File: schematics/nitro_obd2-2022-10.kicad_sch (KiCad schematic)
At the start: 16 parts

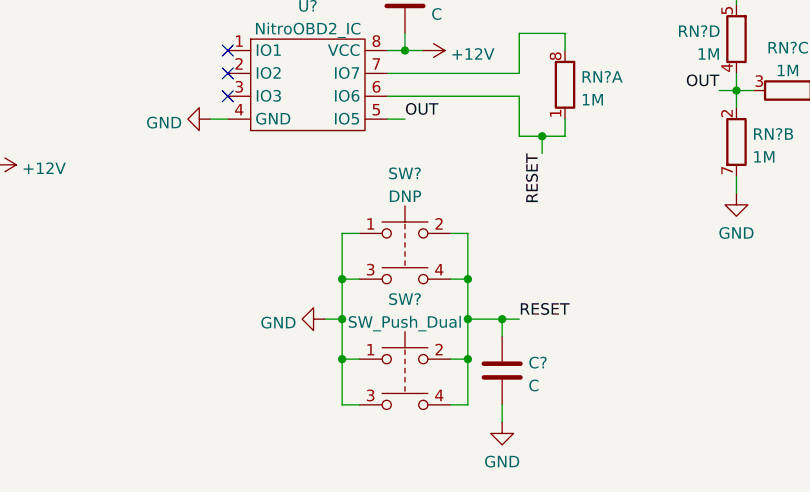
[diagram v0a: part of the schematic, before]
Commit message: Change switch for nitroOBD2 2022-09
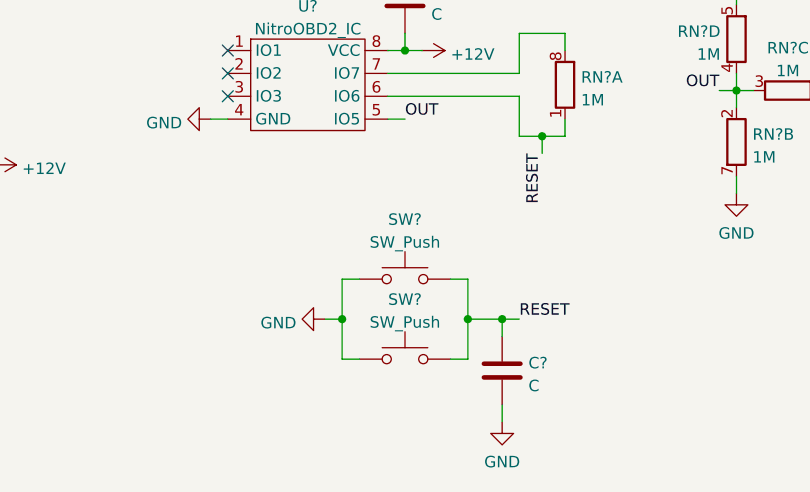
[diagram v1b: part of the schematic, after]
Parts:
- removed SW?: SW_Push_Dual, symbol Switch:SW_Push_Dual
- removed SW?: DNP, symbol Switch:SW_Push_Dual
- added SW? (x2): SW_Push, symbol Switch:SW_Push
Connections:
- net GND: now also SW?.1, SW?.1
- net RESET: now also SW?.2, SW?.2
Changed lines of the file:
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@@
   (junction (at 161.29 123.825) (diameter 0) (color 0 0 0 0)
   )
-  (junction (at 147.32 128.27) (diameter 0) (color 0 0 0 0)
-  )
-  (junction (at 147.32 119.38) (diameter 0) (color 0 0 0 0)
-  )
   (junction (at 191.135 98.425) (diameter 0) (color 0 0 0 0)
   )
@@
   )
   (junction (at 154.305 93.98) (diameter 0) (color 0 0 0 0)
-  )
-  (junction (at 161.29 128.27) (diameter 0) (color 0 0 0 0)
-  )
-  (junction (at 161.29 119.38) (diameter 0) (color 0 0 0 0)
   )
   (junction (at 169.545 103.505) (diameter 0) (color 0 0 0 0)
@@
     (stroke (width 0) (type default) (color 0 0 0 0))
   )
-  (wire (pts (xy 161.29 133.35) (xy 159.385 133.35))
-    (stroke (width 0) (type default) (color 0 0 0 0))
-  )
   (wire (pts (xy 169.545 103.505) (xy 172.085 103.505))
     (stroke (width 0) (type default) (color 0 0 0 0))
@@
     (stroke (width 0) (type default) (color 0 0 0 0))
   )
-  (wire (pts (xy 149.225 114.3) (xy 147.32 114.3))
-    (stroke (width 0) (type default) (color 0 0 0 0))
-  )
-  (wire (pts (xy 161.29 128.27) (xy 161.29 133.35))
-    (stroke (width 0) (type default) (color 0 0 0 0))
-  )
   (wire (pts (xy 154.305 93.98) (xy 156.21 93.98))
     (stroke (width 0) (type default) (color 0 0 0 0))
@@
     (stroke (width 0) (type default) (color 0 0 0 0))
   )
-  (wire (pts (xy 159.385 114.3) (xy 161.29 114.3))
-    (stroke (width 0) (type default) (color 0 0 0 0))
-  )
   (wire (pts (xy 191.135 86.995) (xy 191.135 88.9))
     (stroke (width 0) (type default) (color 0 0 0 0))
@@
     (stroke (width 0) (type default) (color 0 0 0 0))
   )
-  (wire (pts (xy 147.32 133.35) (xy 149.225 133.35))
-    (stroke (width 0) (type default) (color 0 0 0 0))
-  )
   (wire (pts (xy 161.29 119.38) (xy 161.29 123.825))
     (stroke (width 0) (type default) (color 0 0 0 0))
@@
     (stroke (width 0) (type default) (color 0 0 0 0))
   )
-  (wire (pts (xy 147.32 128.27) (xy 147.32 133.35))
-    (stroke (width 0) (type default) (color 0 0 0 0))
-  )
   (wire (pts (xy 204.47 97.79) (xy 204.47 98.425))
     (stroke (width 0) (type default) (color 0 0 0 0))
@@
     (stroke (width 0) (type default) (color 0 0 0 0))
   )
-  (wire (pts (xy 161.29 114.3) (xy 161.29 119.38))
-    (stroke (width 0) (type default) (color 0 0 0 0))
-  )
   (wire (pts (xy 204.47 109.22) (xy 204.47 111.125))
-    (stroke (width 0) (type default) (color 0 0 0 0))
-  )
-  (wire (pts (xy 147.32 114.3) (xy 147.32 119.38))
     (stroke (width 0) (type default) (color 0 0 0 0))
   )
@@
     )
     (pin "1")
-  )
-  (symbol (lib_id "Switch:SW_Push_Dual") (at 154.305 128.27 0) (unit 1)
-    (in_bom yes) (on_board yes) (fields_autoplaced)
-    (property "Reference" "SW?" (id 0) (at 154.305 121.6492 0))
-    (property "Value" "SW_Push_Dual" (id 1) (at 154.305 124.1861 0))
-    (property "Footprint" "" (id 2) (at 154.305 123.19 0)
-      (effects (font (size 1.27 1.27)) hide)
-    )
-    (property "Datasheet" "~" (id 3) (at 154.305 123.19 0)
-      (effects (font (size 1.27 1.27)) hide)
-    )
-    (pin "1")
-    (pin "2")
-    (pin "3")
-    (pin "4")
   )
   (symbol (lib_id "misc_ics:NitroOBD2_IC") (at 143.51 97.79 0) (unit 1)
@@
     (pin "1")
   )
-  (symbol (lib_id "Switch:SW_Push_Dual") (at 154.305 114.3 0) (unit 1)
-    (in_bom yes) (on_board yes) (fields_autoplaced)
-    (property "Reference" "SW?" (id 0) (at 154.305 107.6792 0))
-    (property "Value" "DNP" (id 1) (at 154.305 110.2161 0))
-    (property "Footprint" "" (id 2) (at 154.305 109.22 0)
-      (effects (font (size 1.27 1.27)) hide)
-    )
-    (property "Datasheet" "~" (id 3) (at 154.305 109.22 0)
-      (effects (font (size 1.27 1.27)) hide)
-    )
-    (pin "1")
-    (pin "2")
-    (pin "3")
-    (pin "4")
-  )
   (symbol (lib_id "power:+12V") (at 191.135 86.995 0) (unit 1)
     (in_bom yes) (on_board yes) (fields_autoplaced)
@@
     )
     (pin "1")
+  )
+  (symbol (lib_id "Switch:SW_Push") (at 154.305 119.38 0) (unit 1)
+    (in_bom yes) (on_board yes) (fields_autoplaced)
+    (property "Reference" "SW?" (id 0) (at 154.305 112.7592 0))
+    (property "Value" "SW_Push" (id 1) (at 154.305 115.2961 0))
+    (property "Footprint" "" (id 2) (at 154.305 114.3 0)
+      (effects (font (size 1.27 1.27)) hide)
+    )
+    (property "Datasheet" "~" (id 3) (at 154.305 114.3 0)
+      (effects (font (size 1.27 1.27)) hide)
+    )
+    (pin "1")
+    (pin "2")
+  )
+  (symbol (lib_id "Switch:SW_Push") (at 154.305 128.27 0) (unit 1)
+    (in_bom yes) (on_board yes) (fields_autoplaced)
+    (property "Reference" "SW?" (id 0) (at 154.305 121.6492 0))
+    (property "Value" "SW_Push" (id 1) (at 154.305 124.1861 0))
+    (property "Footprint" "" (id 2) (at 154.305 123.19 0)
+      (effects (font (size 1.27 1.27)) hide)
+    )
+    (property "Datasheet" "~" (id 3) (at 154.305 123.19 0)
+      (effects (font (size 1.27 1.27)) hide)
+    )
+    (pin "1")
+    (pin "2")
   )
   (symbol (lib_id "Device:LED") (at 204.47 105.41 90) (mirror x) (unit 1)
@@
       (reference "RN?") (unit 4) (value "1M") (footprint "")
     )
-    (path "/4a957199-98ca-4d7c-847f-f79ccd0d485c"
-      (reference "SW?") (unit 1) (value "SW_Push_Dual") (footprint "")
-    )
-    (path "/da89d813-e669-4b77-9a4b-1d281c279ba8"
-      (reference "SW?") (unit 1) (value "DNP") (footprint "")
+    (path "/df0c7818-7f02-4c3d-9906-b3ee4d910b10"
+      (reference "SW?") (unit 1) (value "SW_Push") (footprint "")
+    )
+    (path "/e3f5d89d-015c-4144-b939-911526431744"
+      (reference "SW?") (unit 1) (value "SW_Push") (footprint "")
     )
     (path "/51947fb1-f892-4830-93a8-2e54da9ee49f"

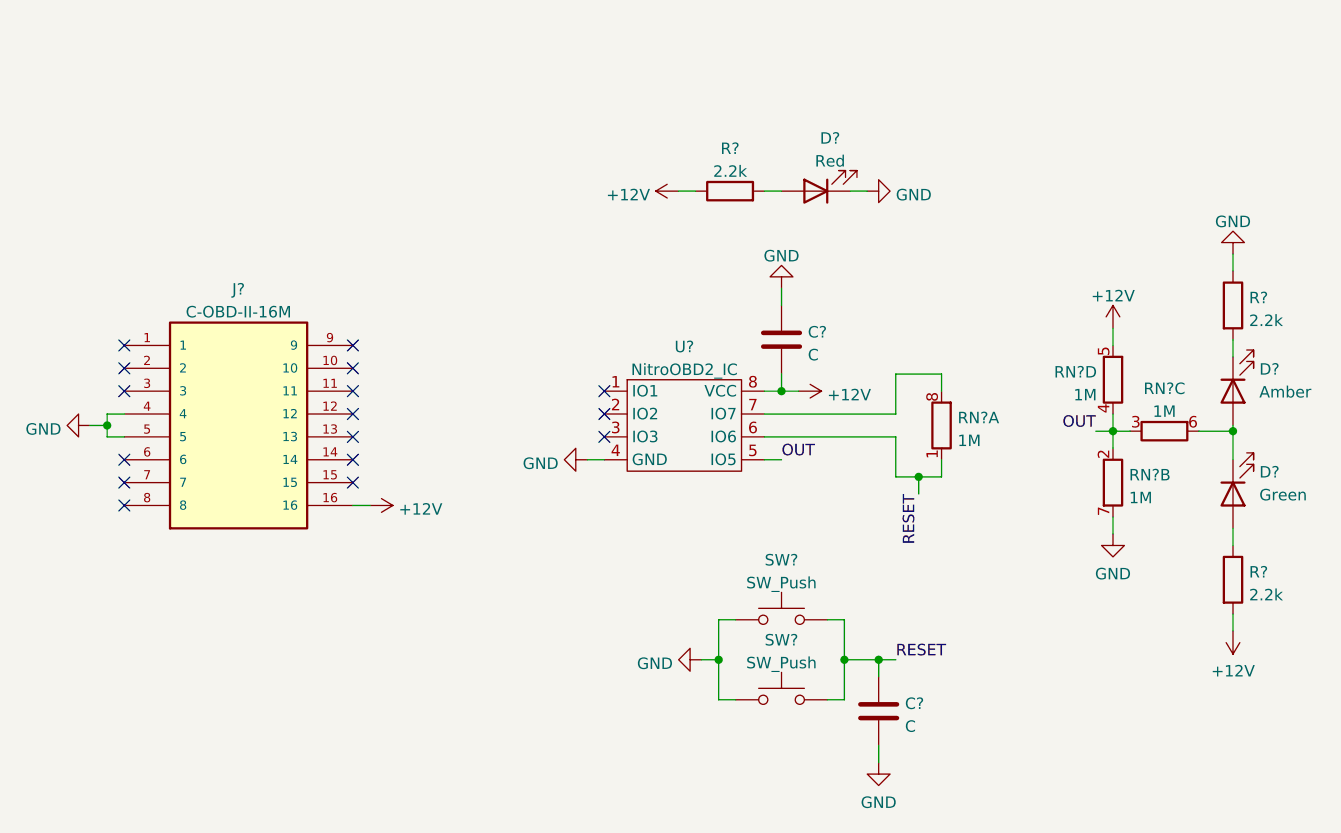
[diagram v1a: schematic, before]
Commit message: Update yellow flasher info and schematic
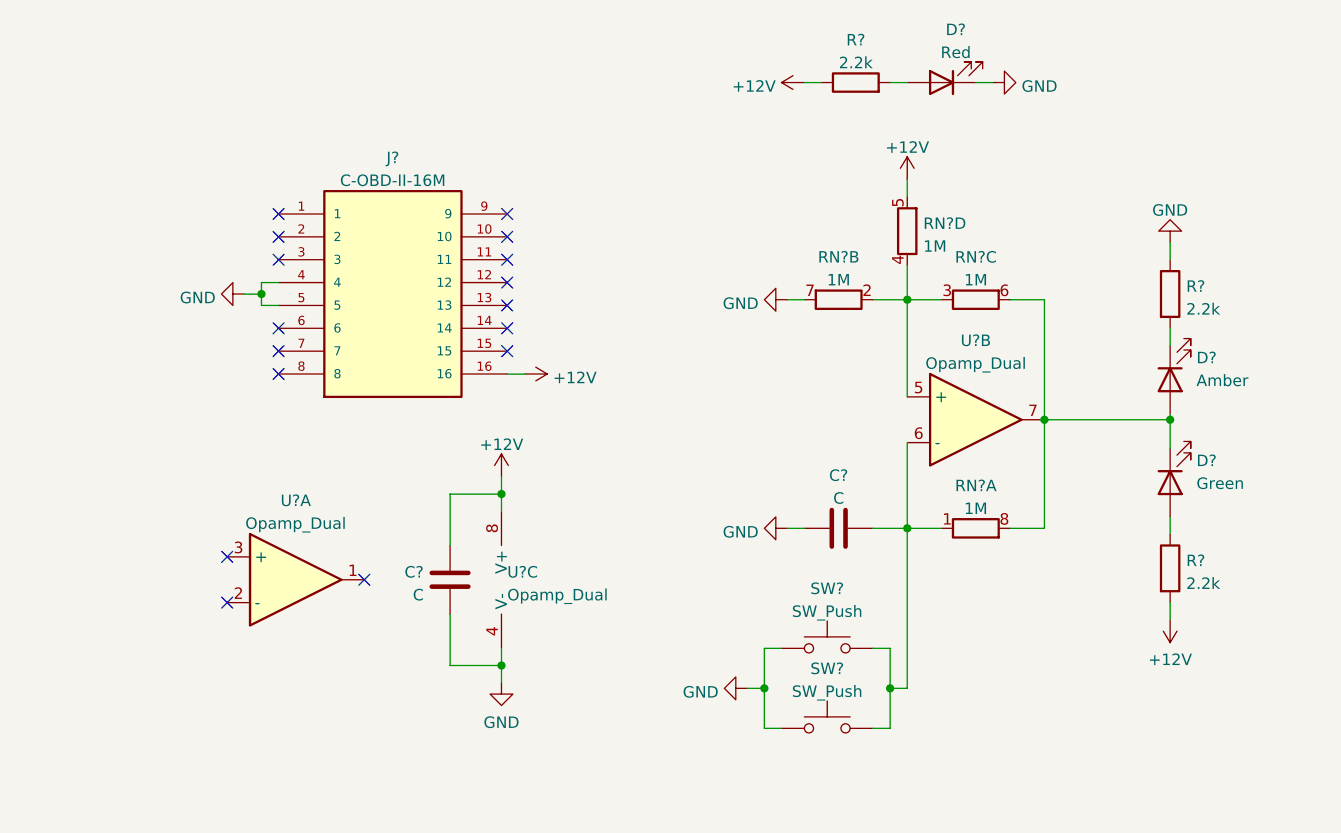
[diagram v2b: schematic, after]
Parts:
- removed U?: NitroOBD2_IC, symbol misc_ics:NitroOBD2_IC
- added U? (x3): Opamp_Dual, symbol Device:Opamp_Dual
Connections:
- net +12V: now also U?.8 (V+)
- net GND: now also C?.1, U?.4 (V-); no longer C?.2
- net at RN?.8 (R1.2): now also D?.1 (K), D?.2 (A), RN?.6 (R3.2), U?.7
- net OUT: no longer names the net of RN?.2 (R2.1), RN?.3 (R3.1), RN?.4 (R4.1)
- net OUT: now also U?.5 (+)
- net RESET: no longer names the net of RN?.1 (R1.1), SW?.2, SW?.2
- net RESET: now also C?.2, U?.6 (-); no longer C?.1
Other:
- moved on the sheet: C?, D?, J?, R?, RN?A, RN?B, RN?C, RN?D, SW?
